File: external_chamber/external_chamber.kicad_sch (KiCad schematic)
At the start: 15 parts, among them J1 Conn_01x02_Socket, J2 Conn_01x07_Socket, J3 Conn_01x08_Socket, J4 Conn_01x05_Socket, J5 Conn_01x02_Socket, J6 Conn_01x08_Socket, J7 Conn_01x08_Socket, J8 Conn_01x06_Socket, J9 Conn_01x02_Socket, U1 CY8CKIT-059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

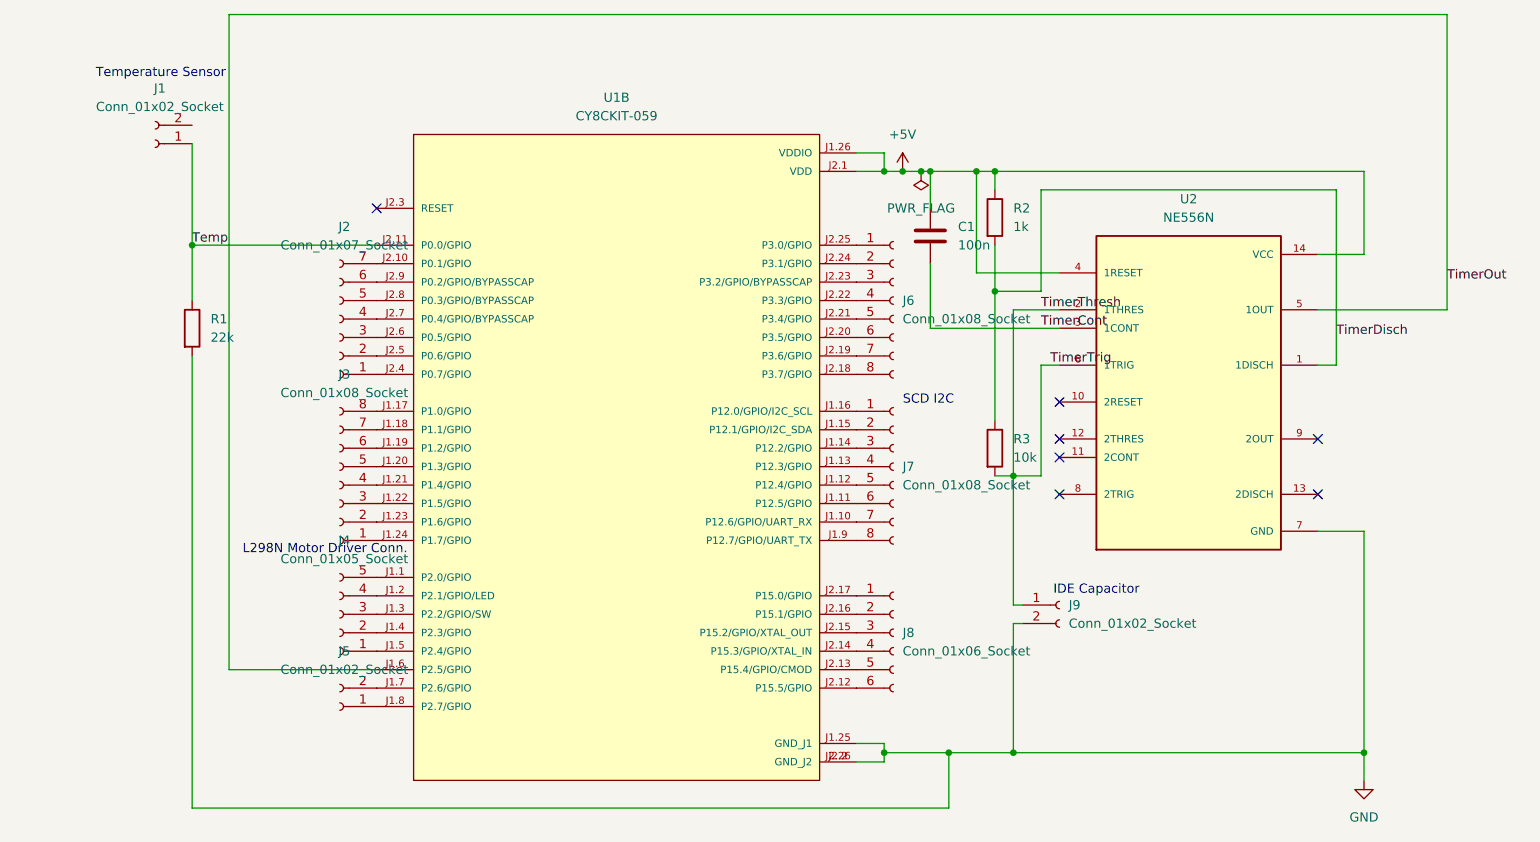
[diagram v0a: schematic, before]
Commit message: Updated heater controls and uploaded re-design of external chamber PCB
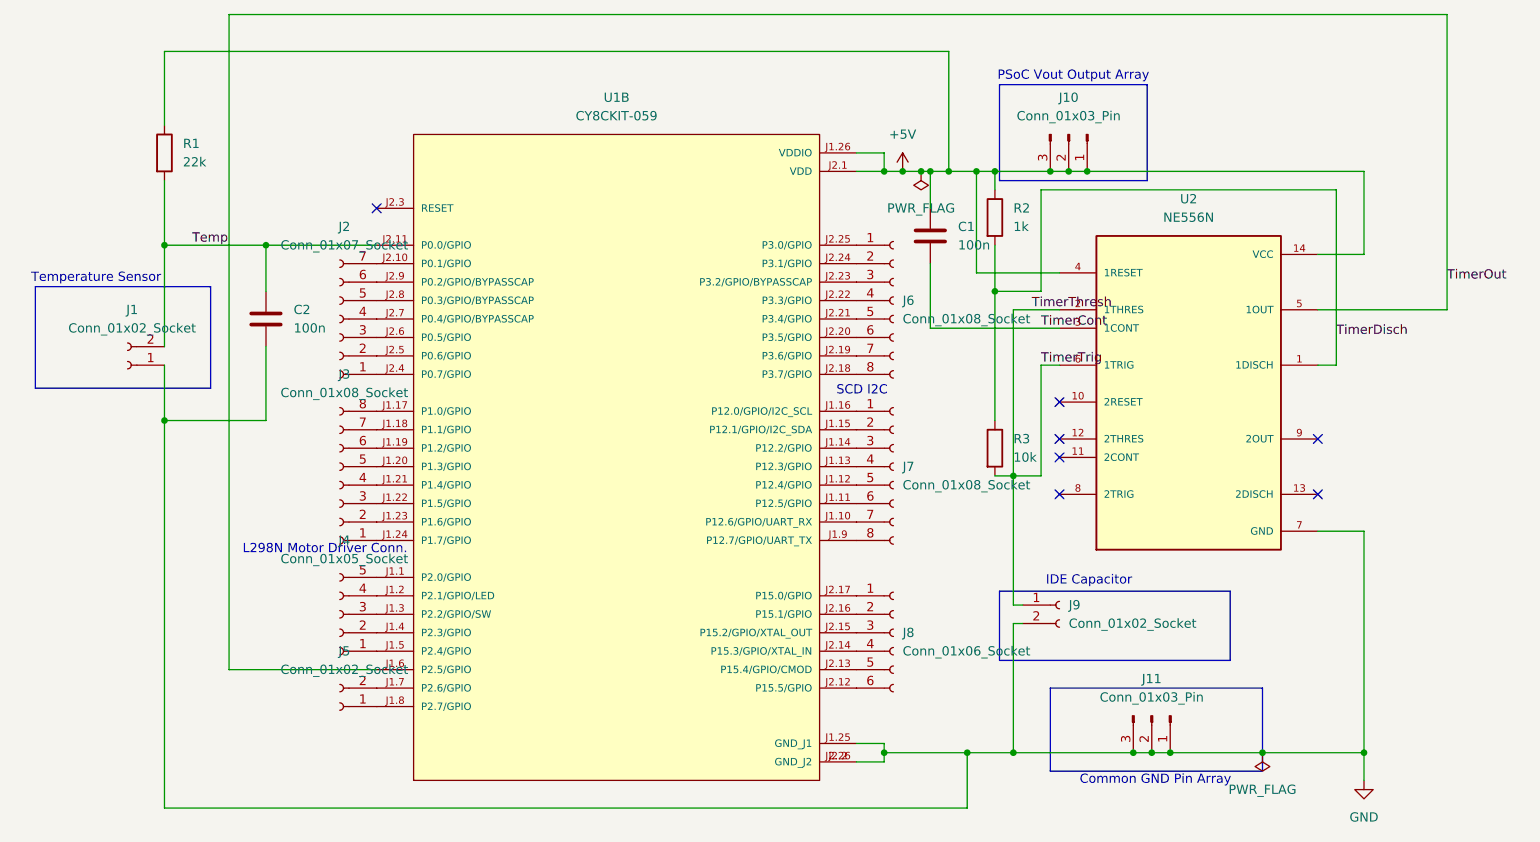
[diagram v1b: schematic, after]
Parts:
- added C2: 100n, Capacitor_THT:C_Disc_D5.0mm_W2.5mm_P5.00mm, symbol Device:C
- added J10, J11: Conn_01x03_Pin, Connector_PinSocket_2.54mm:PinSocket_1x03_P2.54mm_Vertical, symbol Connector:Conn_01x03_Pin
- J7: footprint Connector_PinSocket_2.54mm:PinSocket_1x08_P2.54mm_Vertical -> Connector_PinHeader_2.54mm:PinHeader_1x08_P2.54mm_Vertical
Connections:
- net +5V: now also R1.1, J10.1 (Pin_1), J10.2 (Pin_2), J10.3 (Pin_3)
- net GND: now also J1.1 (Pin_1), C2.2, J11.1 (Pin_1), J11.2 (Pin_2), J11.3 (Pin_3); no longer R1.2
- net Temp: now also J1.2 (Pin_2), R1.2, C2.1; no longer J1.1 (Pin_1), R1.1
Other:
- note added: "Common GND Pin Array"
- note added: "PSoC Vout Output Array"
- company: (none) -> Monash University Malaysia
- title: (none) -> External Gas Chamber Circuit
- moved on the sheet: J1, R1
